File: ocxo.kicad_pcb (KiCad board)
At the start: 2 copper layers, 50 x 50 mm, 21 parts, among them J1 Conn_01x02, J2 Conn_01x01, J3 Conn_Coaxial, J4 Conn_01x01, J5 Conn_01x01, J6 Conn_01x01, J7 Conn_Coaxial, Q1 ENE3311 OCXO, U1 KA78M05_TO252, U2 LM4140

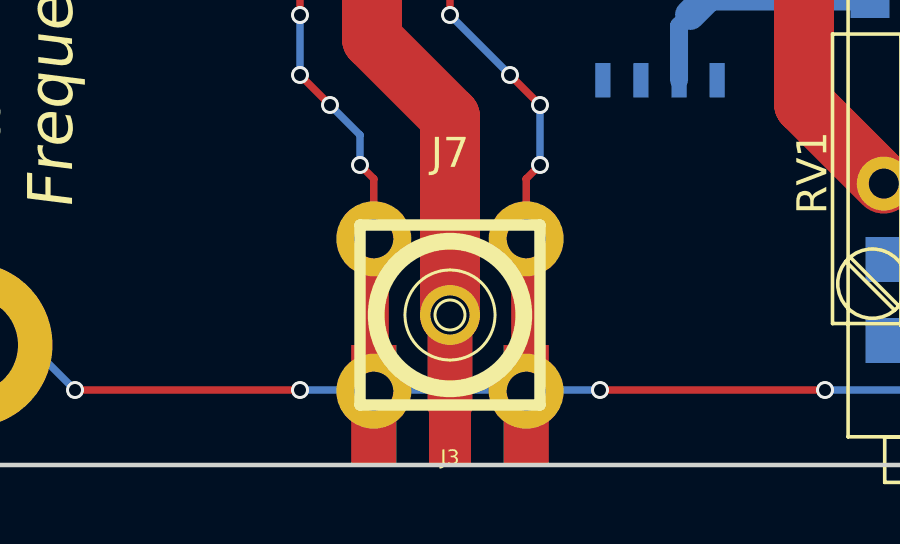
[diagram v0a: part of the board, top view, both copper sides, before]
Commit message: adding OCXO 3D model, 3D screen captures
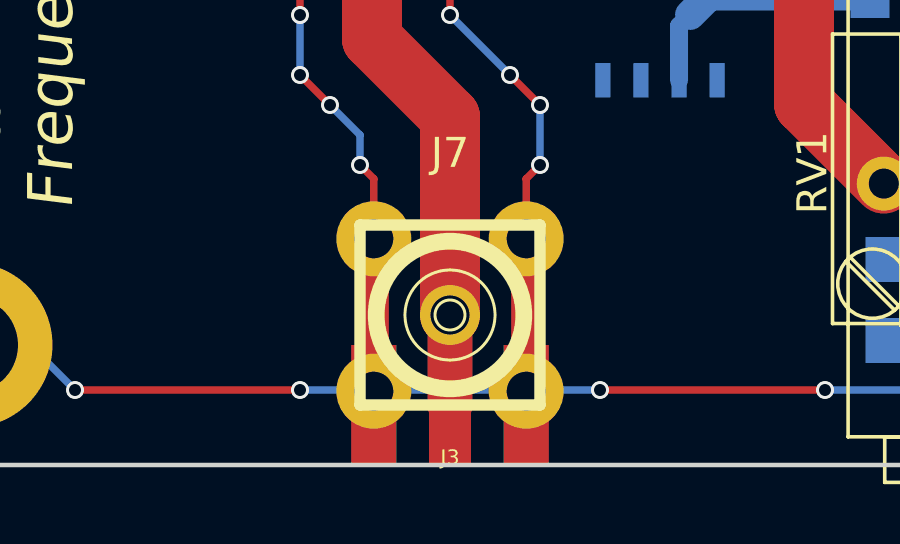
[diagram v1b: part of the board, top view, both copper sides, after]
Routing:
- net GND: track 261.4 -> 271.5 mm
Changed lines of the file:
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@@
     (thickness 1.6)
     (drawings 8)
-    (tracks 192)
+    (tracks 194)
     (zones 0)
     (modules 21)
@@
     (pad 2 thru_hole circle (at 0 9.525) (size 2.5 2.5) (drill 0.8) (layers *.Cu *.Mask)
       (net 2 GND))
+    (model ../../../../../../Users/Marco/Documents/Kicad/modules/ENE3311.pretty/ENE3311.wrl
+      (at (xyz 0 0 0))
+      (scale (xyz 0.38 0.38 0.38))
+      (rotate (xyz 0 0 0))
+    )
   )
   (module Resistors_SMD:R_0805_HandSoldering (layer B.Cu)
@@
   (segment (start 109.29 60.7) (end 113.7 60.7) (width 1.5) (layer B.Cu) (net 1))
   (segment (start 113.7 60.7) (end 114 61) (width 1.5) (layer B.Cu) (net 1))
+  (segment (start 97.46 92.54) (end 97.46 87.46) (width 1) (layer B.Cu) (net 2))
+  (segment (start 102.54 92.54) (end 102.54 87.46) (width 1) (layer B.Cu) (net 2))
   (segment (start 97.46 87.46) (end 97.46 92.54) (width 1) (layer F.Cu) (net 2))
   (segment (start 102.54 87.46) (end 102.54 92.54) (width 1) (layer F.Cu) (net 2))
